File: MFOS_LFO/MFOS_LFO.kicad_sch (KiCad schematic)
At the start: 105 parts, among them J1 Conn_01x01, J10 Conn_01x01, J11 Conn_01x01, J12 Conn_01x01, J13 Conn_01x01, J14 Conn_01x01, J15 Conn_01x01, J16 Conn_01x01, J17 Conn_01x01, J18 Conn_01x01, J2 Conn_01x01, J3 Conn_01x01, J4 Conn_01x01, J5 Conn_01x01, J6 Conn_01x01, J7 Conn_01x01, J8 Conn_01x01, J9 Conn_01x01, Q1 2N3904, Q2 2N3904, Q3 2N3906, Q4 BF245C, Q5 BF245C, Q6 2N3904, U1 TL072, U2 TL082, U3 LM13700, U4 TL082, U5 TL082, U6 TL082

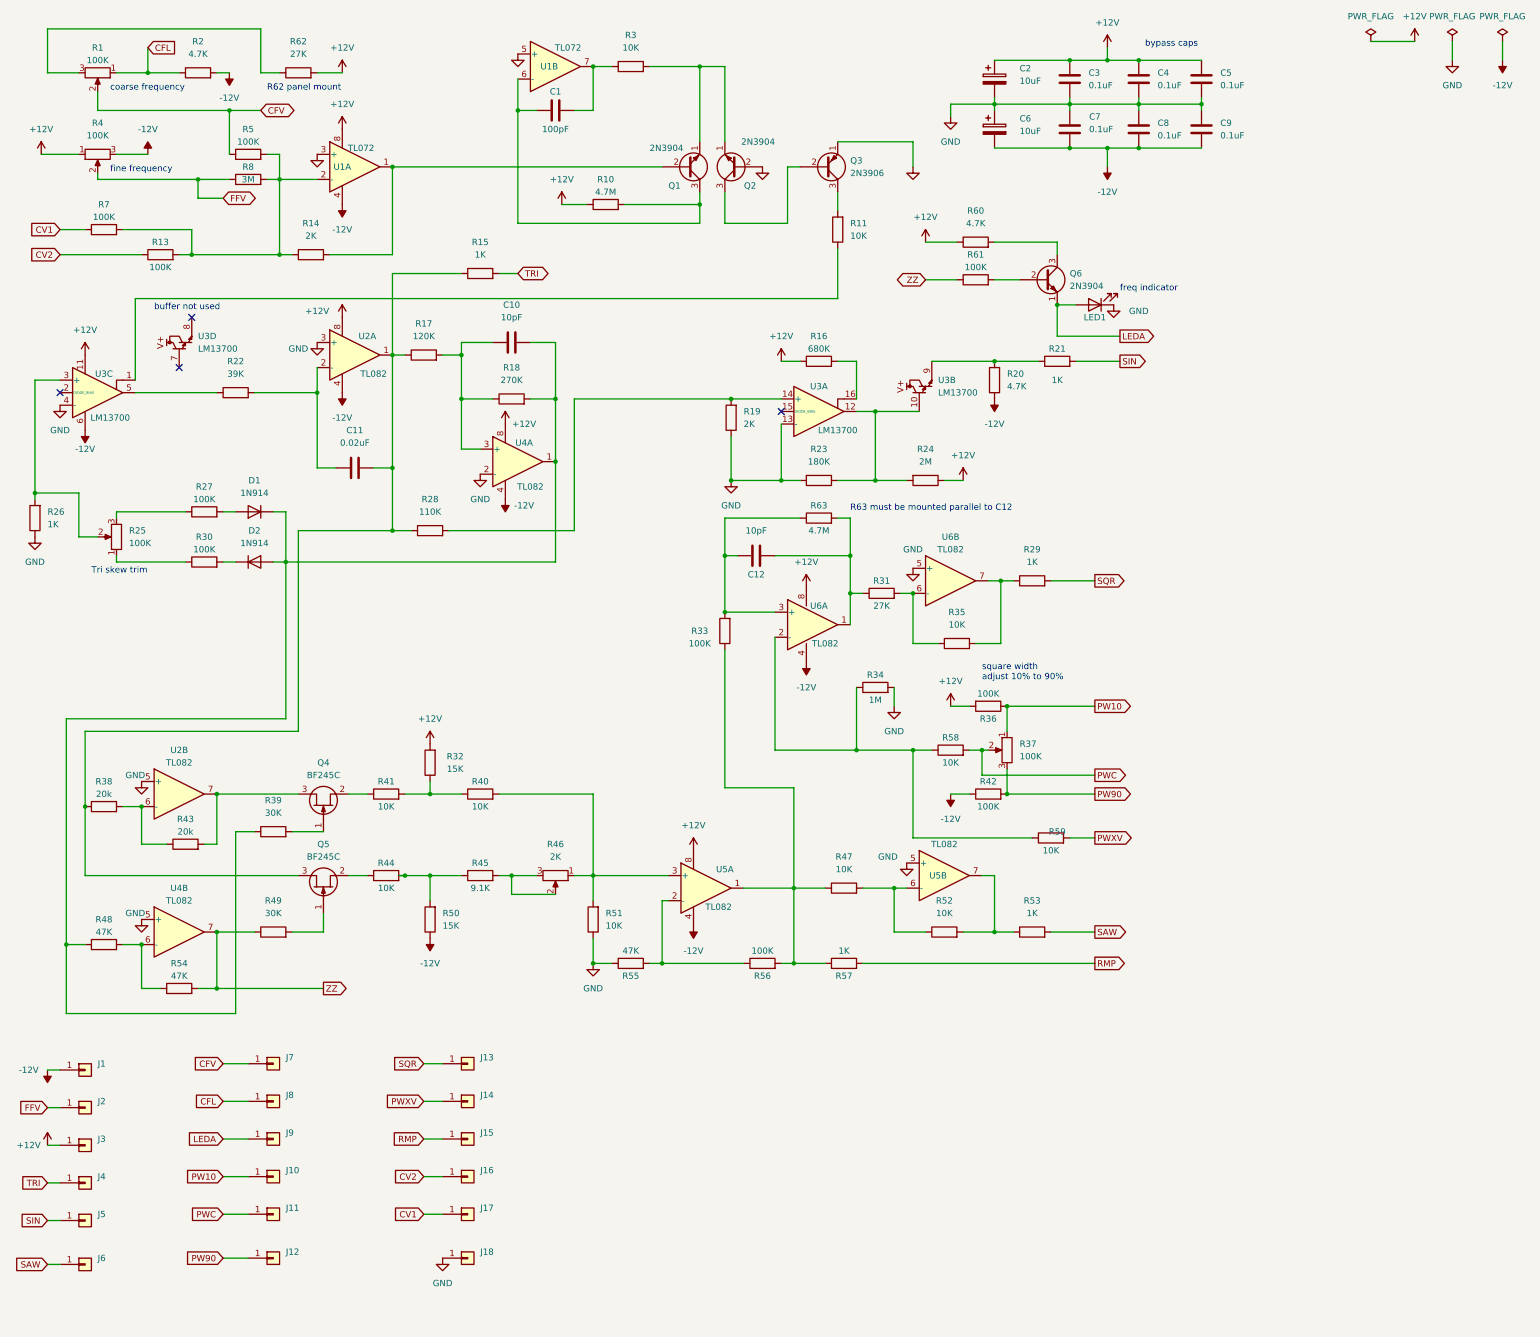
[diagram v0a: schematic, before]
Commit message: Updated BOM, renamed VCO > MFOS_VCO
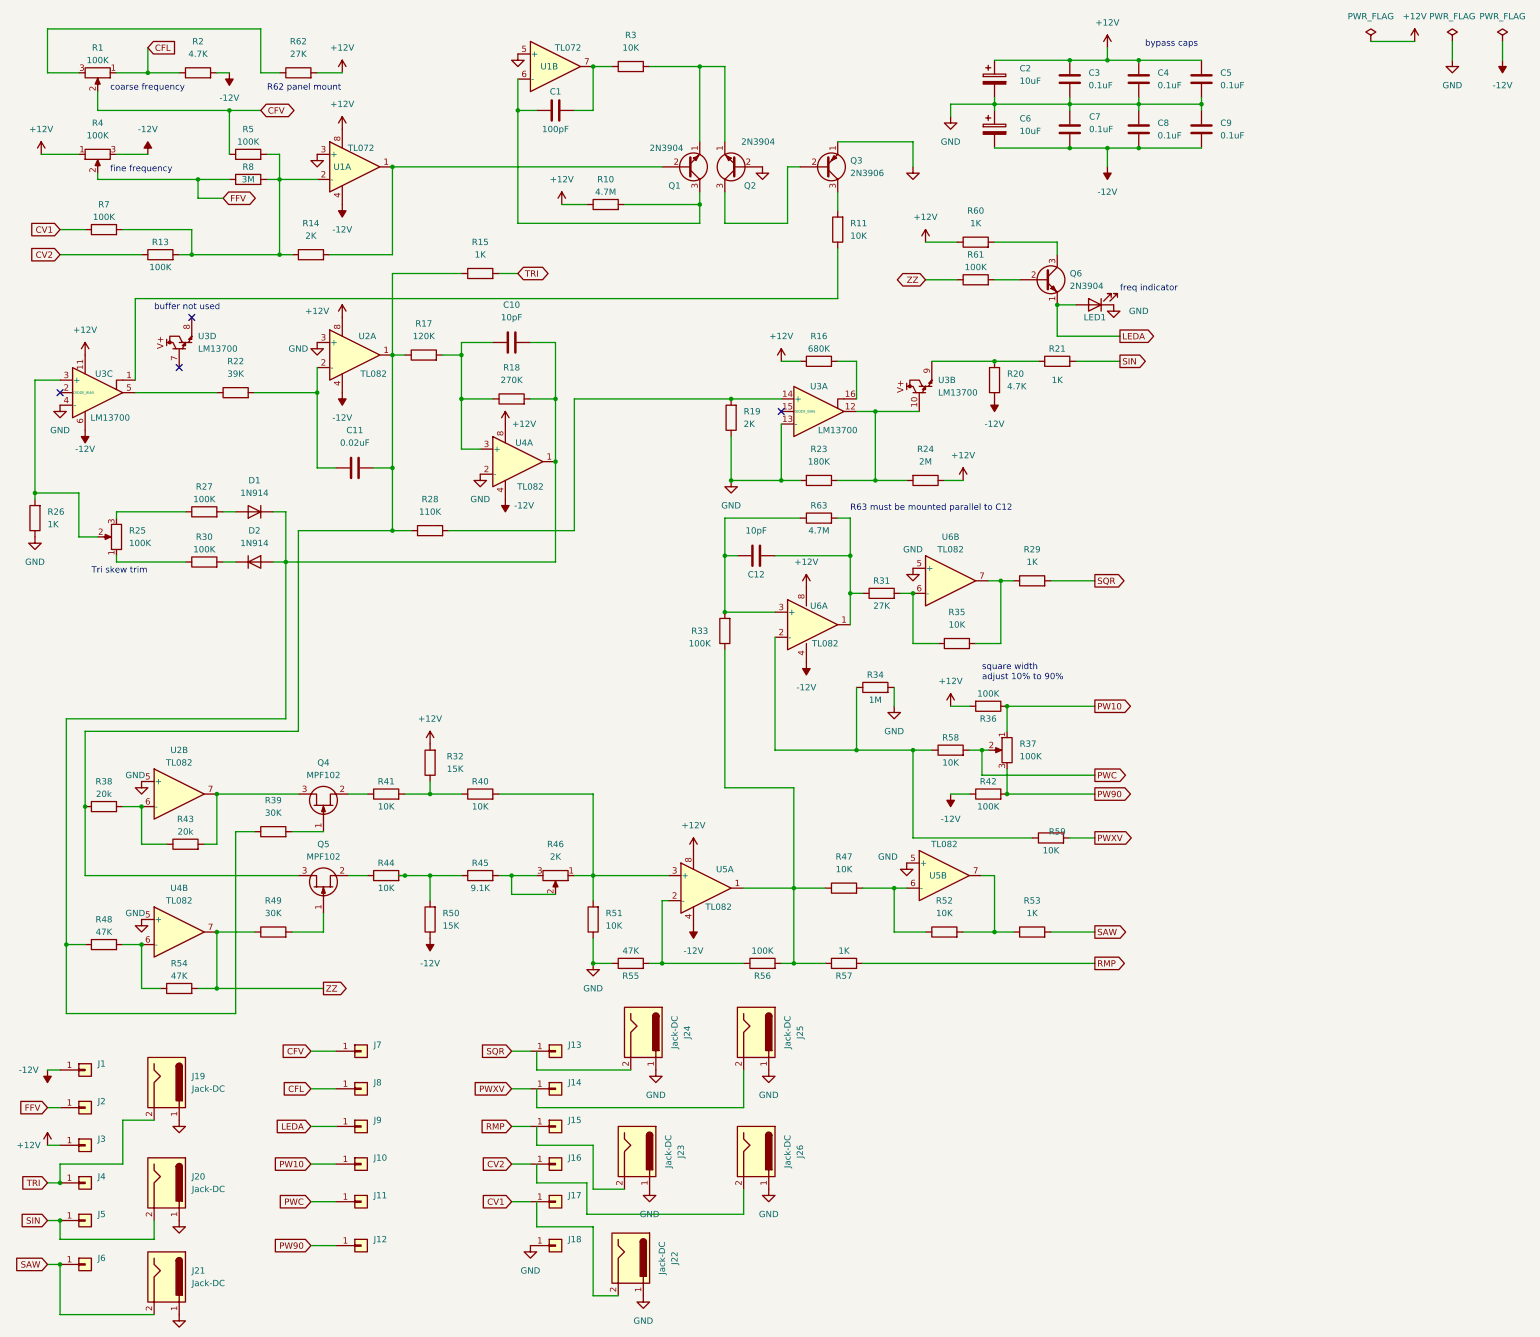
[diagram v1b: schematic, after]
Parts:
- added J19, J20, J21, J22, J23, J24, J25, J26: Jack-DC, symbol Connector:Jack-DC
- Q4, Q5: value BF245C -> MPF102
- R60: value 4.7K -> 1K
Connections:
- net GND: now also J19.1, J20.1, J21.1, J22.1, J23.1, J24.1, J25.1, J26.1
- net SAW: now also J21.2
- net SIN: now also J20.2
- net TRI: now also J19.2
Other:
- moved on the sheet: J10, J11, J12, J13, J14, J15, J16, J17, J18, J7, J8, J9

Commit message: Revision until and with audio mixer complete
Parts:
- removed R25: 100K, symbol Device:R_Potentiometer
- removed R46: 2K, symbol Device:R_Potentiometer
- added R25: 100K, symbol Device:R_Potentiometer_Trim
- added R46: 2K, symbol Device:R_Potentiometer_Trim
- J1, J10, J11, J12, J13, J14, J15, J16, J17, J18, J2, J3, J4, J5, J6, J7, J8, J9: now left out of the parts list
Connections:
- net at R27.1: now also R25.1
- net at R40.2, R51.2, U5.3 (+): now also R46.1
- net at R26.2, U3.3 (+): now also R25.2
- net at R30.1: now also R25.3
- net at R45.2: now also R46.2, R46.3
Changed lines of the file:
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@@
   )
   (symbol (lib_id "Connector_Generic:Conn_01x01") (at 83.82 233.68 0) (unit 1)
-    (in_bom yes) (on_board yes) (fields_autoplaced)
+    (in_bom no) (on_board yes) (fields_autoplaced)
     (property "Reference" "J8" (id 0) (at 86.36 232.4099 0)
       (effects (font (size 1.27 1.27)) (justify left))
@@
   )
   (symbol (lib_id "Connector_Generic:Conn_01x01") (at 83.82 226.06 0) (unit 1)
-    (in_bom yes) (on_board yes) (fields_autoplaced)
+    (in_bom no) (on_board yes) (fields_autoplaced)
     (property "Reference" "J7" (id 0) (at 86.36 224.7899 0)
       (effects (font (size 1.27 1.27)) (justify left))
@@
   )
   (symbol (lib_id "Connector_Generic:Conn_01x01") (at 123.19 241.3 0) (unit 1)
-    (in_bom yes) (on_board yes) (fields_autoplaced)
+    (in_bom no) (on_board yes) (fields_autoplaced)
     (property "Reference" "J15" (id 0) (at 125.73 240.0299 0)
       (effects (font (size 1.27 1.27)) (justify left))
@@
   )
   (symbol (lib_id "Connector_Generic:Conn_01x01") (at 123.19 233.68 0) (unit 1)
-    (in_bom yes) (on_board yes) (fields_autoplaced)
+    (in_bom no) (on_board yes) (fields_autoplaced)
     (property "Reference" "J14" (id 0) (at 125.73 232.4099 0)
       (effects (font (size 1.27 1.27)) (justify left))
@@
   )
   (symbol (lib_id "Connector_Generic:Conn_01x01") (at 123.19 248.92 0) (unit 1)
-    (in_bom yes) (on_board yes) (fields_autoplaced)
+    (in_bom no) (on_board yes) (fields_autoplaced)
     (property "Reference" "J16" (id 0) (at 125.73 247.6499 0)
       (effects (font (size 1.27 1.27)) (justify left))
@@
   )
   (symbol (lib_id "Connector_Generic:Conn_01x01") (at 27.94 229.87 0) (unit 1)
-    (in_bom yes) (on_board yes) (fields_autoplaced)
+    (in_bom no) (on_board yes) (fields_autoplaced)
     (property "Reference" "J1" (id 0) (at 30.48 228.5999 0)
       (effects (font (size 1.27 1.27)) (justify left))
@@
   )
   (symbol (lib_id "Connector_Generic:Conn_01x01") (at 123.19 256.54 0) (unit 1)
-    (in_bom yes) (on_board yes) (fields_autoplaced)
+    (in_bom no) (on_board yes) (fields_autoplaced)
     (property "Reference" "J17" (id 0) (at 125.73 255.2699 0)
       (effects (font (size 1.27 1.27)) (justify left))
@@
     (pin "1")
   )
+  (symbol (lib_id "Device:R_Potentiometer_Trim") (at 34.29 121.92 0) (mirror y) (unit 1)
+    (in_bom yes) (on_board yes) (fields_autoplaced)
+    (property "Reference" "R25" (id 0) (at 36.83 121.9199 0)
+      (effects (font (size 1.27 1.27)) (justify right))
+    )
+    (property "Value" "100K" (id 1) (at 36.83 123.1899 0)
+      (effects (font (size 1.27 1.27)) (justify right))
+    )
+    (property "Footprint" "" (id 2) (at 34.29 121.92 0)
+      (effects (font (size 1.27 1.27)) hide)
+    )
+    (property "Datasheet" "~" (id 3) (at 34.29 121.92 0)
+      (effects (font (size 1.27 1.27)) hide)
+    )
+    (pin "1")
+    (pin "2")
+    (pin "3")
+  )
   (symbol (lib_id "Connector:Jack-DC") (at 163.83 222.25 270) (unit 1)
     (in_bom yes) (on_board yes) (fields_autoplaced)
@@
   )
   (symbol (lib_id "Connector_Generic:Conn_01x01") (at 27.94 260.35 0) (unit 1)
-    (in_bom yes) (on_board yes) (fields_autoplaced)
+    (in_bom no) (on_board yes) (fields_autoplaced)
     (property "Reference" "J5" (id 0) (at 30.48 259.0799 0)
       (effects (font (size 1.27 1.27)) (justify left))
@@
   )
   (symbol (lib_id "Connector_Generic:Conn_01x01") (at 27.94 269.24 0) (unit 1)
-    (in_bom yes) (on_board yes) (fields_autoplaced)
+    (in_bom no) (on_board yes) (fields_autoplaced)
     (property "Reference" "J6" (id 0) (at 30.48 267.9699 0)
       (effects (font (size 1.27 1.27)) (justify left))
@@
   )
   (symbol (lib_id "Connector_Generic:Conn_01x01") (at 83.82 248.92 0) (unit 1)
-    (in_bom yes) (on_board yes) (fields_autoplaced)
+    (in_bom no) (on_board yes) (fields_autoplaced)
     (property "Reference" "J10" (id 0) (at 86.36 247.6499 0)
       (effects (font (size 1.27 1.27)) (justify left))
@@
     (pin "1")
   )
-  (symbol (lib_id "Device:R_Potentiometer") (at 34.29 121.92 180) (unit 1)
-    (in_bom yes) (on_board yes) (fields_autoplaced)
-    (property "Reference" "R25" (id 0) (at 36.83 120.6499 0)
-      (effects (font (size 1.27 1.27)) (justify right))
-    )
-    (property "Value" "100K" (id 1) (at 36.83 123.1899 0)
-      (effects (font (size 1.27 1.27)) (justify right))
-    )
-    (property "Footprint" "" (id 2) (at 34.29 121.92 0)
-      (effects (font (size 1.27 1.27)) hide)
-    )
-    (property "Datasheet" "~" (id 3) (at 34.29 121.92 0)
-      (effects (font (size 1.27 1.27)) hide)
-    )
-    (pin "1")
-    (pin "2")
-    (pin "3")
-  )
   (symbol (lib_id "Device:R") (at 107.95 190.5 90) (unit 1)
     (in_bom yes) (on_board yes)
@@
     (pin "1")
   )
-  (symbol (lib_id "Device:R_Potentiometer") (at 123.19 190.5 270) (unit 1)
-    (in_bom yes) (on_board yes) (fields_autoplaced)
-    (property "Reference" "R46" (id 0) (at 123.19 184.15 90))
-    (property "Value" "2K" (id 1) (at 123.19 186.69 90))
-    (property "Footprint" "" (id 2) (at 123.19 190.5 0)
-      (effects (font (size 1.27 1.27)) hide)
-    )
-    (property "Datasheet" "~" (id 3) (at 123.19 190.5 0)
-      (effects (font (size 1.27 1.27)) hide)
-    )
-    (pin "1")
-    (pin "2")
-    (pin "3")
-  )
   (symbol (lib_id "Device:R") (at 97.79 120.65 90) (unit 1)
     (in_bom yes) (on_board yes) (fields_autoplaced)
@@
   )
   (symbol (lib_id "Connector_Generic:Conn_01x01") (at 83.82 256.54 0) (unit 1)
-    (in_bom yes) (on_board yes) (fields_autoplaced)
+    (in_bom no) (on_board yes) (fields_autoplaced)
     (property "Reference" "J11" (id 0) (at 86.36 255.2699 0)
       (effects (font (size 1.27 1.27)) (justify left))
@@
   )
   (symbol (lib_id "Connector_Generic:Conn_01x01") (at 83.82 265.43 0) (unit 1)
-    (in_bom yes) (on_board yes) (fields_autoplaced)
+    (in_bom no) (on_board yes) (fields_autoplaced)
     (property "Reference" "J12" (id 0) (at 86.36 264.1599 0)
       (effects (font (size 1.27 1.27)) (justify left))
@@
   )
   (symbol (lib_id "Connector_Generic:Conn_01x01") (at 27.94 252.73 0) (unit 1)
-    (in_bom yes) (on_board yes) (fields_autoplaced)
+    (in_bom no) (on_board yes) (fields_autoplaced)
     (property "Reference" "J4" (id 0) (at 30.48 251.4599 0)
       (effects (font (size 1.27 1.27)) (justify left))
@@
   )
   (symbol (lib_id "Connector_Generic:Conn_01x01") (at 27.94 237.49 0) (unit 1)
-    (in_bom yes) (on_board yes) (fields_autoplaced)
+    (in_bom no) (on_board yes) (fields_autoplaced)
     (property "Reference" "J2" (id 0) (at 30.48 236.2199 0)
       (effects (font (size 1.27 1.27)) (justify left))
@@
   )
   (symbol (lib_id "Connector_Generic:Conn_01x01") (at 83.82 241.3 0) (unit 1)
-    (in_bom yes) (on_board yes) (fields_autoplaced)
+    (in_bom no) (on_board yes) (fields_autoplaced)
     (property "Reference" "J9" (id 0) (at 86.36 240.0299 0)
       (effects (font (size 1.27 1.27)) (justify left))
@@
   )
   (symbol (lib_id "Connector_Generic:Conn_01x01") (at 27.94 245.11 0) (unit 1)
-    (in_bom yes) (on_board yes) (fields_autoplaced)
+    (in_bom no) (on_board yes) (fields_autoplaced)
     (property "Reference" "J3" (id 0) (at 30.48 243.8399 0)
       (effects (font (size 1.27 1.27)) (justify left))
@@
     (pin "1")
   )
+  (symbol (lib_id "Device:R_Potentiometer_Trim") (at 123.19 190.5 270) (unit 1)
+    (in_bom yes) (on_board yes) (fields_autoplaced)
+    (property "Reference" "R46" (id 0) (at 123.19 184.15 90))
+    (property "Value" "2K" (id 1) (at 123.19 186.69 90))
+    (property "Footprint" "" (id 2) (at 123.19 190.5 0)
+      (effects (font (size 1.27 1.27)) hide)
+    )
+    (property "Datasheet" "~" (id 3) (at 123.19 190.5 0)
+      (effects (font (size 1.27 1.27)) hide)
+    )
+    (pin "1")
+    (pin "2")
+    (pin "3")
+  )
   (symbol (lib_id "power:GND") (at 140.97 275.59 0) (unit 1)
     (in_bom yes) (on_board yes) (fields_autoplaced)
@@
   )
   (symbol (lib_id "Connector_Generic:Conn_01x01") (at 123.19 226.06 0) (unit 1)
-    (in_bom yes) (on_board yes) (fields_autoplaced)
+    (in_bom no) (on_board yes) (fields_autoplaced)
     (property "Reference" "J13" (id 0) (at 125.73 224.7899 0)
       (effects (font (size 1.27 1.27)) (justify left))
@@
   )
   (symbol (lib_id "Connector_Generic:Conn_01x01") (at 123.19 265.43 0) (unit 1)
-    (in_bom yes) (on_board yes) (fields_autoplaced)
+    (in_bom no) (on_board yes) (fields_autoplaced)
     (property "Reference" "J18" (id 0) (at 125.73 264.1599 0)
       (effects (font (size 1.27 1.27)) (justify left))
@@
       (reference "R24") (unit 1) (value "2M") (footprint "")
     )
-    (path "/84b5e43c-3941-4ea0-b3f3-dccff04b70f0"
+    (path "/5b419ab8-a3a9-44ee-bdc5-c6e032b42b74"
       (reference "R25") (unit 1) (value "100K") (footprint "")
     )
@@
       (reference "R45") (unit 1) (value "9.1K") (footprint "")
     )
-    (path "/87ab137c-e15f-440c-8717-eeb74a3a4a92"
+    (path "/d26b1c79-9014-47f5-ab0f-2abdb8dbc4f1"
       (reference "R46") (unit 1) (value "2K") (footprint "")
     )

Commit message: Designs adapted for BOM
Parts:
- R25, R46: symbol Device:R_Potentiometer_Trim -> dhk:R_Potentiometer_Trim
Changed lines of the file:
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@@
     (pin "1")
   )
-  (symbol (lib_id "Device:R_Potentiometer_Trim") (at 34.29 121.92 0) (mirror y) (unit 1)
+  (symbol (lib_id "dhk:R_Potentiometer_Trim") (at 34.29 121.92 0) (mirror y) (unit 1)
     (in_bom yes) (on_board yes) (fields_autoplaced)
     (property "Reference" "R25" (id 0) (at 36.83 121.9199 0)
@@
     (pin "1")
   )
-  (symbol (lib_id "Device:R_Potentiometer_Trim") (at 123.19 190.5 270) (unit 1)
+  (symbol (lib_id "dhk:R_Potentiometer_Trim") (at 123.19 190.5 270) (unit 1)
     (in_bom yes) (on_board yes) (fields_autoplaced)
     (property "Reference" "R46" (id 0) (at 123.19 184.15 90))
